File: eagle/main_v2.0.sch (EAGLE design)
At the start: 101 parts, among them IC1 74HC257D, IC2 PCA9530, IC3 RAC04, IC4 CS8416, IC5 MCP130-300I/SN, IC6 MAX1724, K1 G6A-234P, T1 BC847, T2 BC857, T3 BC847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

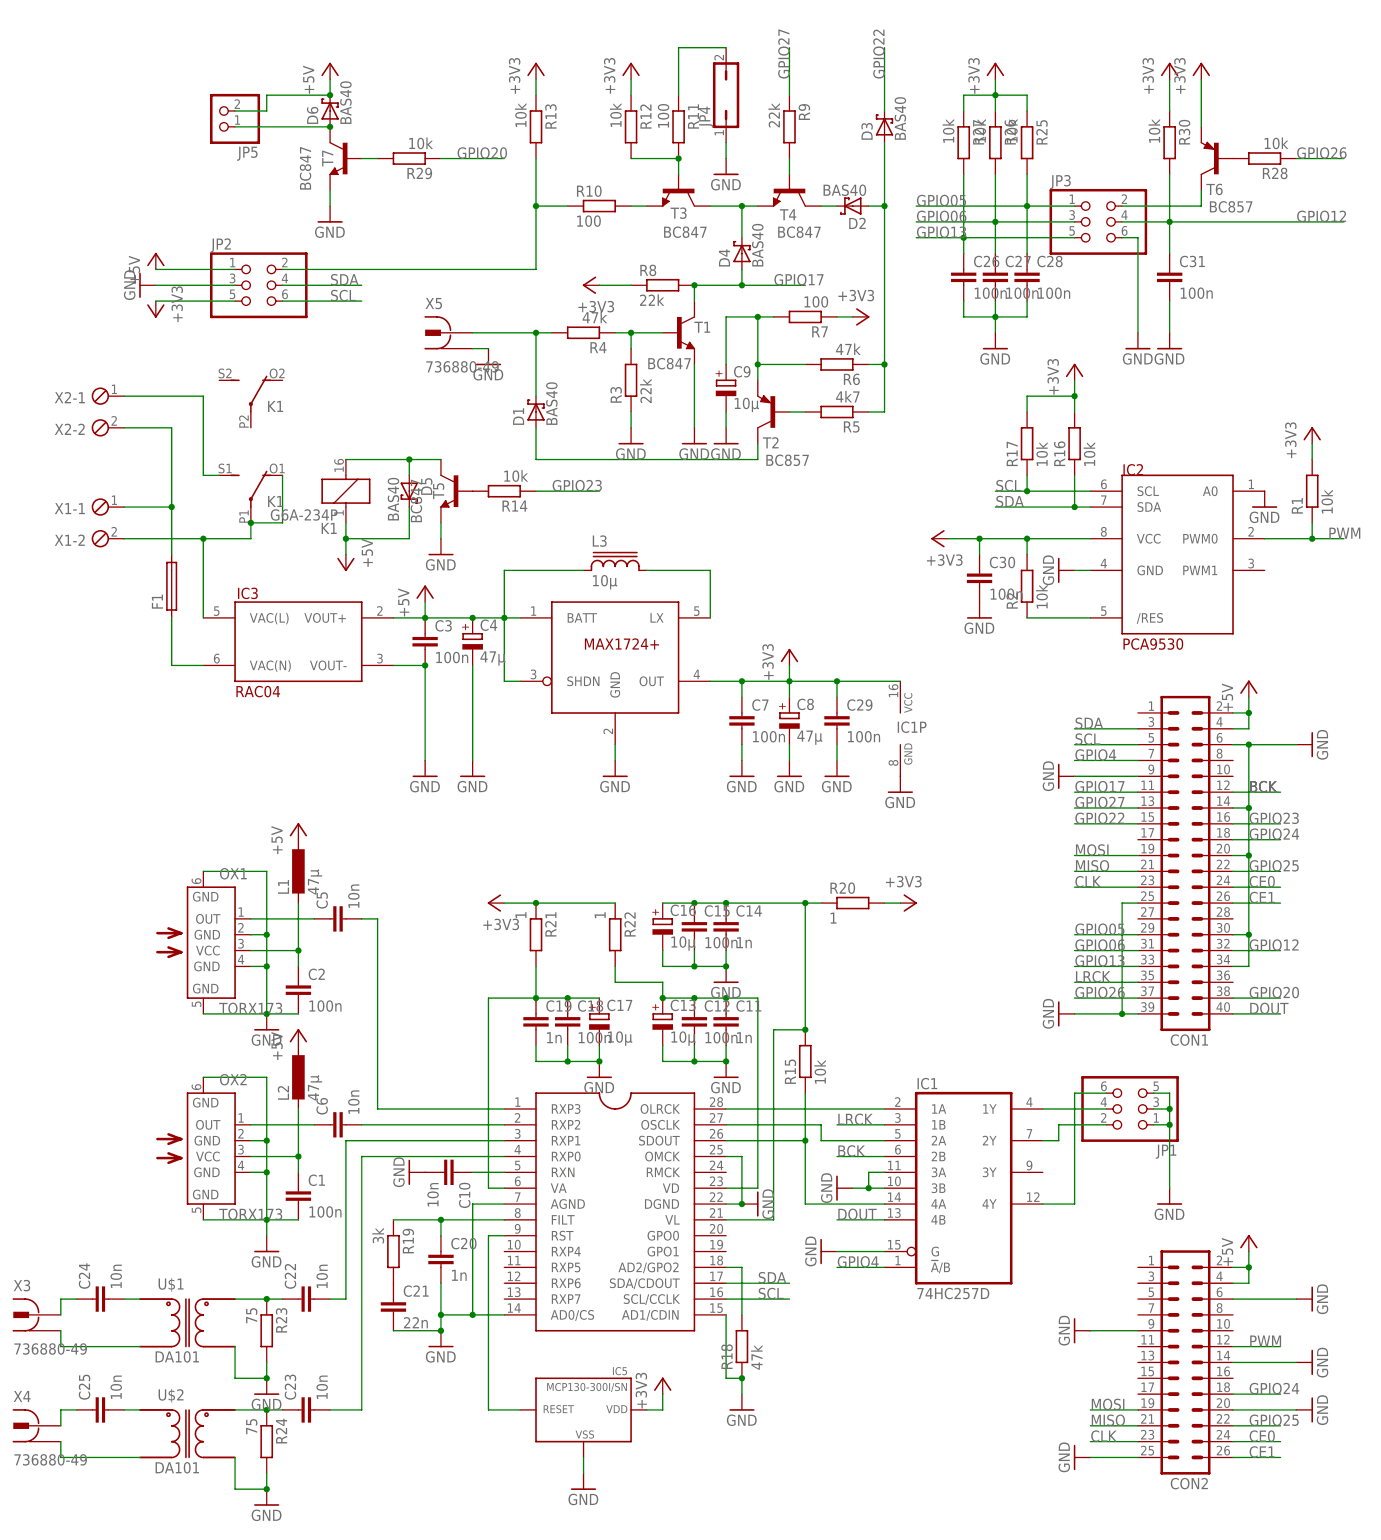
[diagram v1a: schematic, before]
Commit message: Eagle V2.0: 3.3V Step-Down-Wandler ersetzt und Fehler behoben. Keine weiteren Anpassungen mehr nötig.
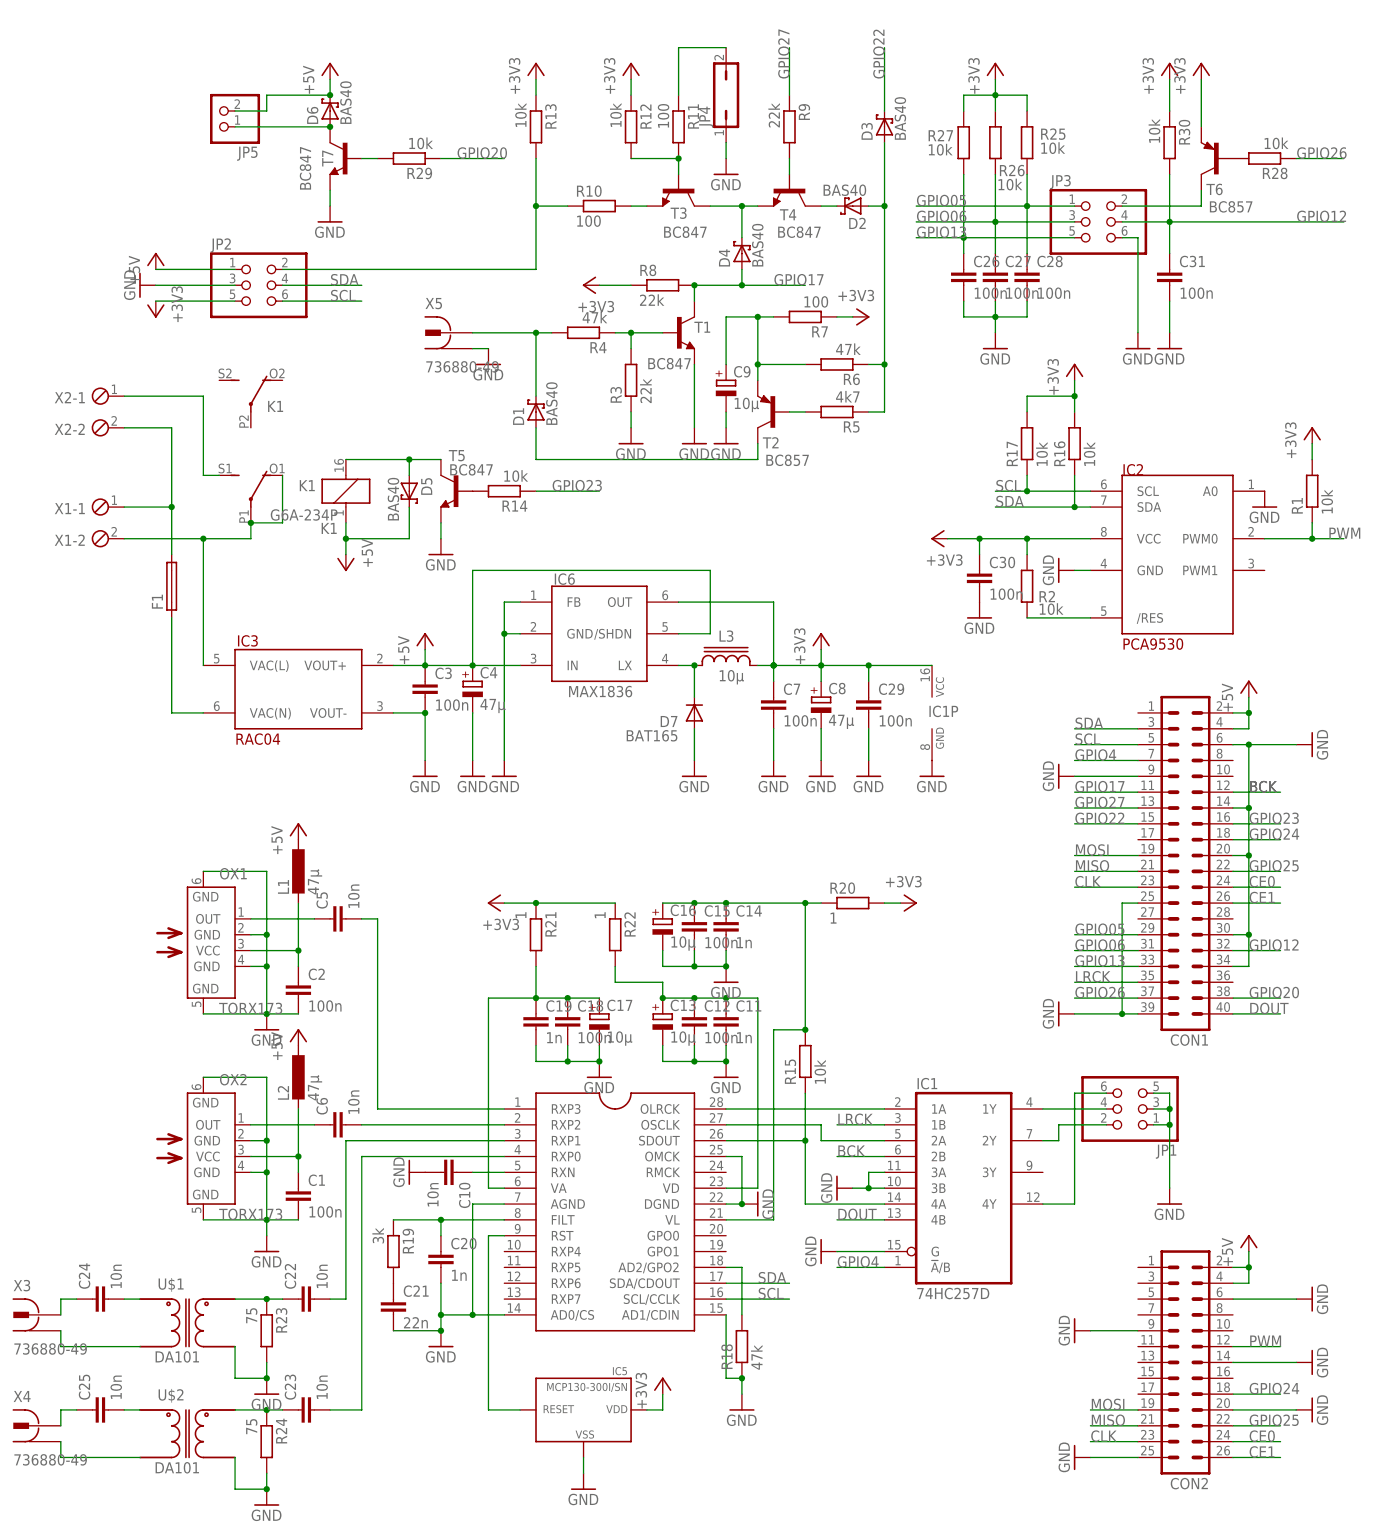
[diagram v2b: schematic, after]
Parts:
- added D7: BAT165, dp_devices:DIODE-SOD-323
- IC6: value MAX1724 -> MAX1836; device MAX1724:MAX1724 -> maxim-5:MAX1836SOT23
- L3: device inductor-coilcraft:DS1608C -> inductor-coilcraft:LPS4018
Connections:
- net +3V3: now also L3.2
- net +5V: now also IC6./SHDN, IC6.IN; no longer IC6.BATT, IC6.SHDN, L3.1
- net GND: now also D7.A, IC6.FB
- net N$28: now also D7.C, L3.1; no longer L3.2
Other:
- moved on the sheet: C29, C3, C4, C7, C8, IC1P, IC3, L3
